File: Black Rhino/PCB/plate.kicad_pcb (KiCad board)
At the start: 2 copper layers, 271.5 x 109.5 mm, 12 parts

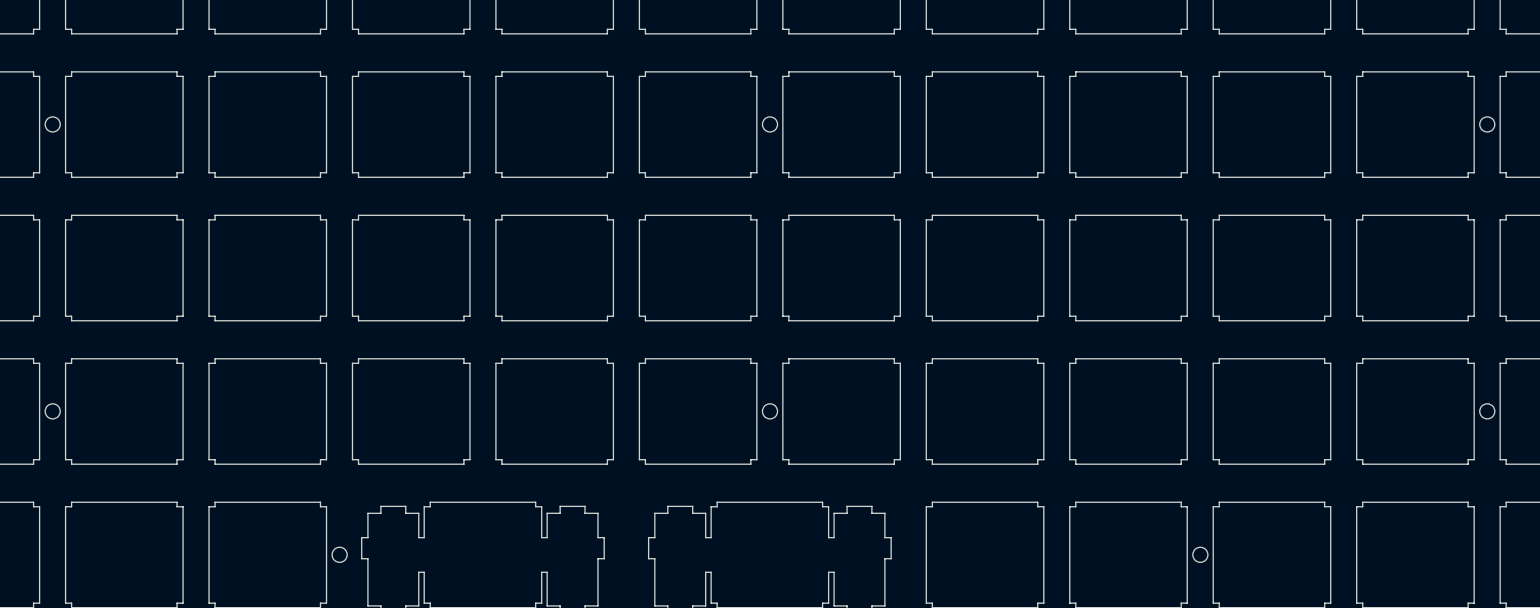
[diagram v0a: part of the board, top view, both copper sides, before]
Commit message: Add Black Rhino-Base & Improve Black Rhino-PCB
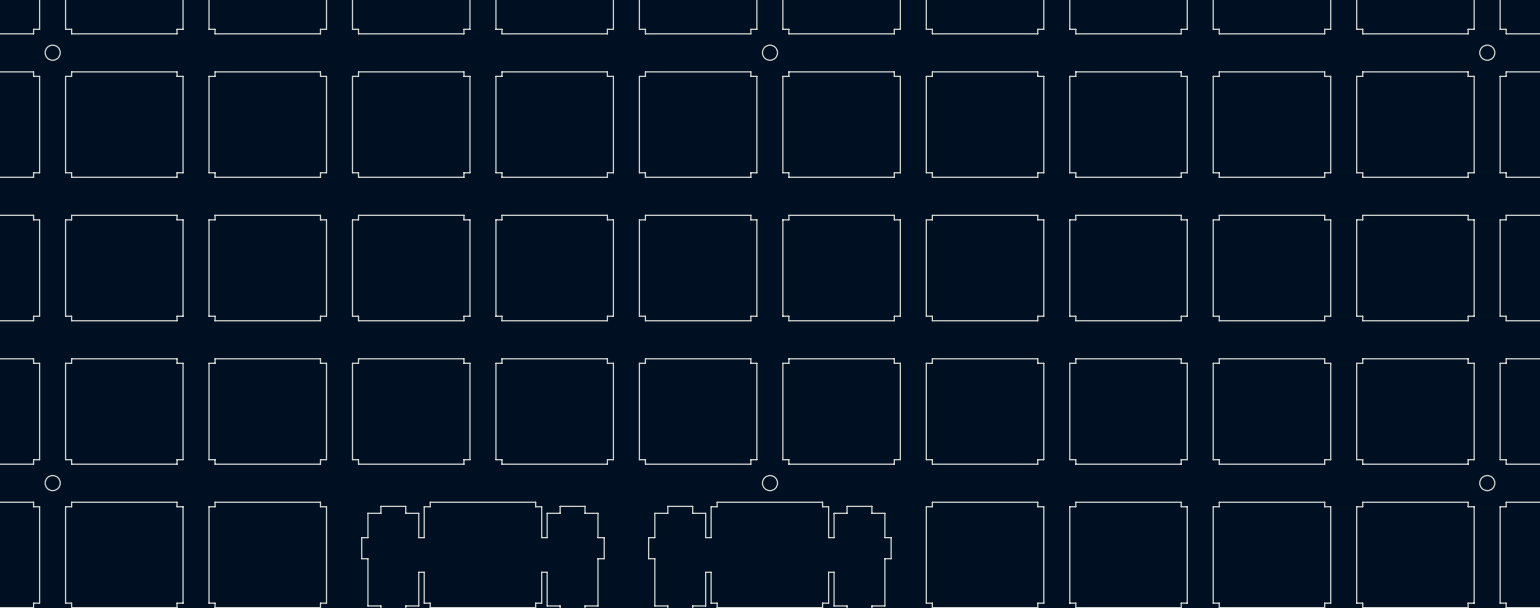
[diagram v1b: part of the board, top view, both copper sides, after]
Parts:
- removed H11, H12: MountingHole, MountingHole:MountingHole_2mm
- moved H10 9.53 mm to (148.4, 138.9)
- moved H5 9.53 mm to (53.2, 81.8)
- moved H6 9.53 mm to (243.7, 81.8)
- moved H7 9.53 mm to (53.2, 138.9)
- moved H8 9.53 mm to (243.7, 138.9)
- moved H9 9.53 mm to (148.4, 81.8)
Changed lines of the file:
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@@
     (tracks 0)
     (zones 0)
-    (modules 12)
+    (modules 10)
     (nets 1)
   )
@@
   )
   (setup
-    (last_trace_width 0.15)
+    (last_trace_width 0.254)
     (user_trace_width 0.15)
     (user_trace_width 0.2)
@@
   )
   (module MountingHole:MountingHole_2mm (layer B.Cu)
-    (at 205.58125 148.43125)
-    (descr "Mounting Hole 2mm, no annular")
-    (tags "mounting hole 2mm no annular")
-    (attr virtual)
-    (fp_text reference H12 (at 0 3.2) (layer B.SilkS)
-      (effects (font (size 1 1) (thickness 0.15)) (justify mirror))
-    )
-    (fp_text value MountingHole (at 0 -3.1) (layer B.Fab)
-      (effects (font (size 1 1) (thickness 0.15)) (justify mirror))
-    )
-    (fp_circle (center 0 0) (end 2.25 0) (layer B.CrtYd) (width 0.05))
-    (fp_circle (center 0 0) (end 2 0) (layer Cmts.User) (width 0.15))
-    (fp_text user %R (at 0.3 0) (layer B.Fab)
-      (effects (font (size 1 1) (thickness 0.15)) (justify mirror))
-    )
-    (pad "" np_thru_hole circle (at 0 0) (size 2 2) (drill 2) (layers *.Cu *.Mask))
-  )
-  (module MountingHole:MountingHole_2mm (layer B.Cu)
-    (at 91.28125 148.43125)
-    (descr "Mounting Hole 2mm, no annular")
-    (tags "mounting hole 2mm no annular")
-    (attr virtual)
-    (fp_text reference H11 (at 0 3.2) (layer B.SilkS)
-      (effects (font (size 1 1) (thickness 0.15)) (justify mirror))
-    )
-    (fp_text value MountingHole (at 0 -3.1) (layer B.Fab)
-      (effects (font (size 1 1) (thickness 0.15)) (justify mirror))
-    )
-    (fp_circle (center 0 0) (end 2.25 0) (layer B.CrtYd) (width 0.05))
-    (fp_circle (center 0 0) (end 2 0) (layer Cmts.User) (width 0.15))
-    (fp_text user %R (at 0.3 0) (layer B.Fab)
-      (effects (font (size 1 1) (thickness 0.15)) (justify mirror))
-    )
-    (pad "" np_thru_hole circle (at 0 0) (size 2 2) (drill 2) (layers *.Cu *.Mask))
-  )
-  (module MountingHole:MountingHole_2mm (layer B.Cu)
-    (at 148.43125 129.38125)
-    (descr "Mounting Hole 2mm, no annular")
-    (tags "mounting hole 2mm no annular")
-    (attr virtual)
-    (fp_text reference H10 (at 0 3.2) (layer B.SilkS)
-      (effects (font (size 1 1) (thickness 0.15)) (justify mirror))
-    )
-    (fp_text value MountingHole (at 0 -3.1) (layer B.Fab)
-      (effects (font (size 1 1) (thickness 0.15)) (justify mirror))
-    )
-    (fp_circle (center 0 0) (end 2.25 0) (layer B.CrtYd) (width 0.05))
-    (fp_circle (center 0 0) (end 2 0) (layer Cmts.User) (width 0.15))
-    (fp_text user %R (at 0.3 0) (layer B.Fab)
-      (effects (font (size 1 1) (thickness 0.15)) (justify mirror))
-    )
-    (pad "" np_thru_hole circle (at 0 0) (size 2 2) (drill 2) (layers *.Cu *.Mask))
-  )
-  (module MountingHole:MountingHole_2mm (layer B.Cu)
-    (at 148.43125 91.28125)
+    (at 148.43125 138.90625)
+    (descr "Mounting Hole 2mm, no annular")
+    (tags "mounting hole 2mm no annular")
+    (attr virtual)
+    (fp_text reference H10 (at 0 -3.175) (layer B.SilkS)
+      (effects (font (size 1 1) (thickness 0.15)) (justify mirror))
+    )
+    (fp_text value MountingHole (at 0 -3.1) (layer B.Fab)
+      (effects (font (size 1 1) (thickness 0.15)) (justify mirror))
+    )
+    (fp_circle (center 0 0) (end 2.25 0) (layer B.CrtYd) (width 0.05))
+    (fp_circle (center 0 0) (end 2 0) (layer Cmts.User) (width 0.15))
+    (fp_text user %R (at 0.3 0) (layer B.Fab)
+      (effects (font (size 1 1) (thickness 0.15)) (justify mirror))
+    )
+    (pad "" np_thru_hole circle (at 0 0) (size 2 2) (drill 2) (layers *.Cu *.Mask))
+  )
+  (module MountingHole:MountingHole_2mm (layer B.Cu)
+    (at 148.43125 81.75625)
     (descr "Mounting Hole 2mm, no annular")
     (tags "mounting hole 2mm no annular")
@@
   )
   (module MountingHole:MountingHole_2mm (layer B.Cu)
-    (at 243.68125 129.38125)
-    (descr "Mounting Hole 2mm, no annular")
-    (tags "mounting hole 2mm no annular")
-    (attr virtual)
-    (fp_text reference H8 (at 0 3.2) (layer B.SilkS)
-      (effects (font (size 1 1) (thickness 0.15)) (justify mirror))
-    )
-    (fp_text value MountingHole (at 0 -3.1) (layer B.Fab)
-      (effects (font (size 1 1) (thickness 0.15)) (justify mirror))
-    )
-    (fp_circle (center 0 0) (end 2.25 0) (layer B.CrtYd) (width 0.05))
-    (fp_circle (center 0 0) (end 2 0) (layer Cmts.User) (width 0.15))
-    (fp_text user %R (at 0.3 0) (layer B.Fab)
-      (effects (font (size 1 1) (thickness 0.15)) (justify mirror))
-    )
-    (pad "" np_thru_hole circle (at 0 0) (size 2 2) (drill 2) (layers *.Cu *.Mask))
-  )
-  (module MountingHole:MountingHole_2mm (layer B.Cu)
-    (at 53.18125 129.38125)
-    (descr "Mounting Hole 2mm, no annular")
-    (tags "mounting hole 2mm no annular")
-    (attr virtual)
-    (fp_text reference H7 (at 0 3.2) (layer B.SilkS)
-      (effects (font (size 1 1) (thickness 0.15)) (justify mirror))
-    )
-    (fp_text value MountingHole (at 0 -3.1) (layer B.Fab)
-      (effects (font (size 1 1) (thickness 0.15)) (justify mirror))
-    )
-    (fp_circle (center 0 0) (end 2.25 0) (layer B.CrtYd) (width 0.05))
-    (fp_circle (center 0 0) (end 2 0) (layer Cmts.User) (width 0.15))
-    (fp_text user %R (at 0.3 0) (layer B.Fab)
-      (effects (font (size 1 1) (thickness 0.15)) (justify mirror))
-    )
-    (pad "" np_thru_hole circle (at 0 0) (size 2 2) (drill 2) (layers *.Cu *.Mask))
-  )
-  (module MountingHole:MountingHole_2mm (layer B.Cu)
-    (at 243.68125 91.28125)
+    (at 243.68125 138.90625)
+    (descr "Mounting Hole 2mm, no annular")
+    (tags "mounting hole 2mm no annular")
+    (attr virtual)
+    (fp_text reference H8 (at 0 -3.175) (layer B.SilkS)
+      (effects (font (size 1 1) (thickness 0.15)) (justify mirror))
+    )
+    (fp_text value MountingHole (at 0 -3.1) (layer B.Fab)
+      (effects (font (size 1 1) (thickness 0.15)) (justify mirror))
+    )
+    (fp_circle (center 0 0) (end 2.25 0) (layer B.CrtYd) (width 0.05))
+    (fp_circle (center 0 0) (end 2 0) (layer Cmts.User) (width 0.15))
+    (fp_text user %R (at 0.3 0) (layer B.Fab)
+      (effects (font (size 1 1) (thickness 0.15)) (justify mirror))
+    )
+    (pad "" np_thru_hole circle (at 0 0) (size 2 2) (drill 2) (layers *.Cu *.Mask))
+  )
+  (module MountingHole:MountingHole_2mm (layer B.Cu)
+    (at 53.18125 138.90625)
+    (descr "Mounting Hole 2mm, no annular")
+    (tags "mounting hole 2mm no annular")
+    (attr virtual)
+    (fp_text reference H7 (at 0 -3.175) (layer B.SilkS)
+      (effects (font (size 1 1) (thickness 0.15)) (justify mirror))
+    )
+    (fp_text value MountingHole (at 0 -3.1) (layer B.Fab)
+      (effects (font (size 1 1) (thickness 0.15)) (justify mirror))
+    )
+    (fp_circle (center 0 0) (end 2.25 0) (layer B.CrtYd) (width 0.05))
+    (fp_circle (center 0 0) (end 2 0) (layer Cmts.User) (width 0.15))
+    (fp_text user %R (at 0.3 0) (layer B.Fab)
+      (effects (font (size 1 1) (thickness 0.15)) (justify mirror))
+    )
+    (pad "" np_thru_hole circle (at 0 0) (size 2 2) (drill 2) (layers *.Cu *.Mask))
+  )
+  (module MountingHole:MountingHole_2mm (layer B.Cu)
+    (at 243.68125 81.75625)
     (descr "Mounting Hole 2mm, no annular")
     (tags "mounting hole 2mm no annular")
@@
   )
   (module MountingHole:MountingHole_2mm (layer B.Cu)
-    (at 53.18125 91.28125)
-    (descr "Mounting Hole 2mm, no annular")
-    (tags "mounting hole 2mm no annular")
+    (at 53.18125 81.75625)
+    (descr "Mounting Hole 2mm, no annular")
+    (tags "mounting hole 2mm no annular")
